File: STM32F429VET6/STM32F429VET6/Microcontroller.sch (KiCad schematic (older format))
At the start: 36 parts

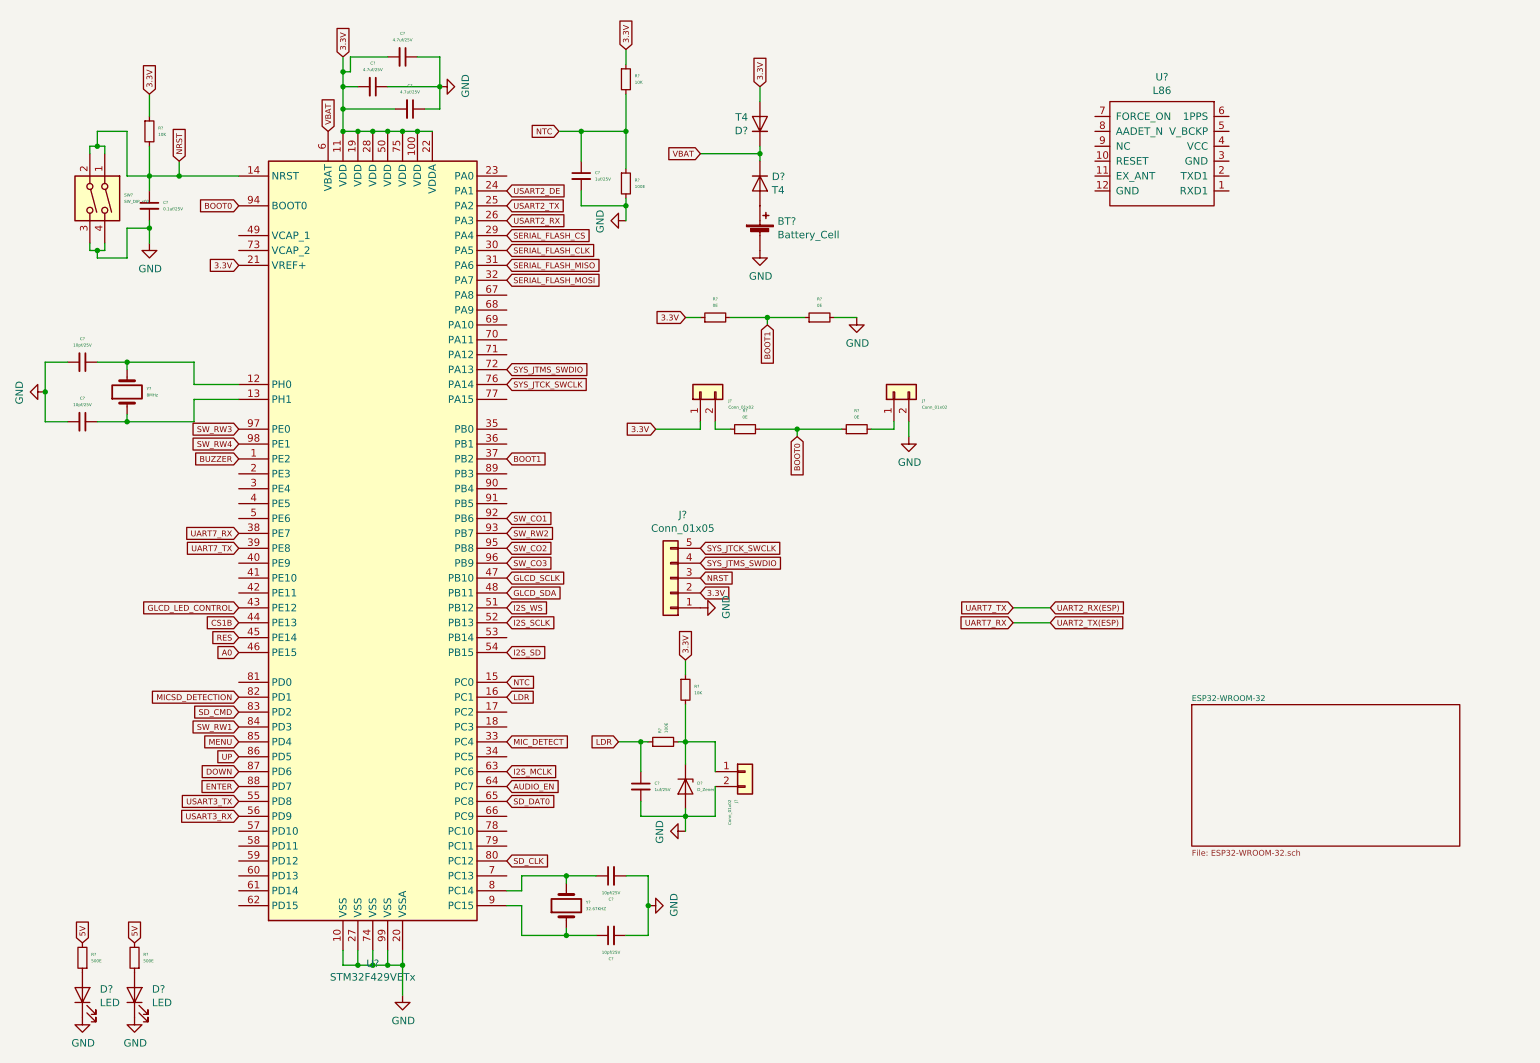
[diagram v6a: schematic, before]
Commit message: Completed GPS module connection
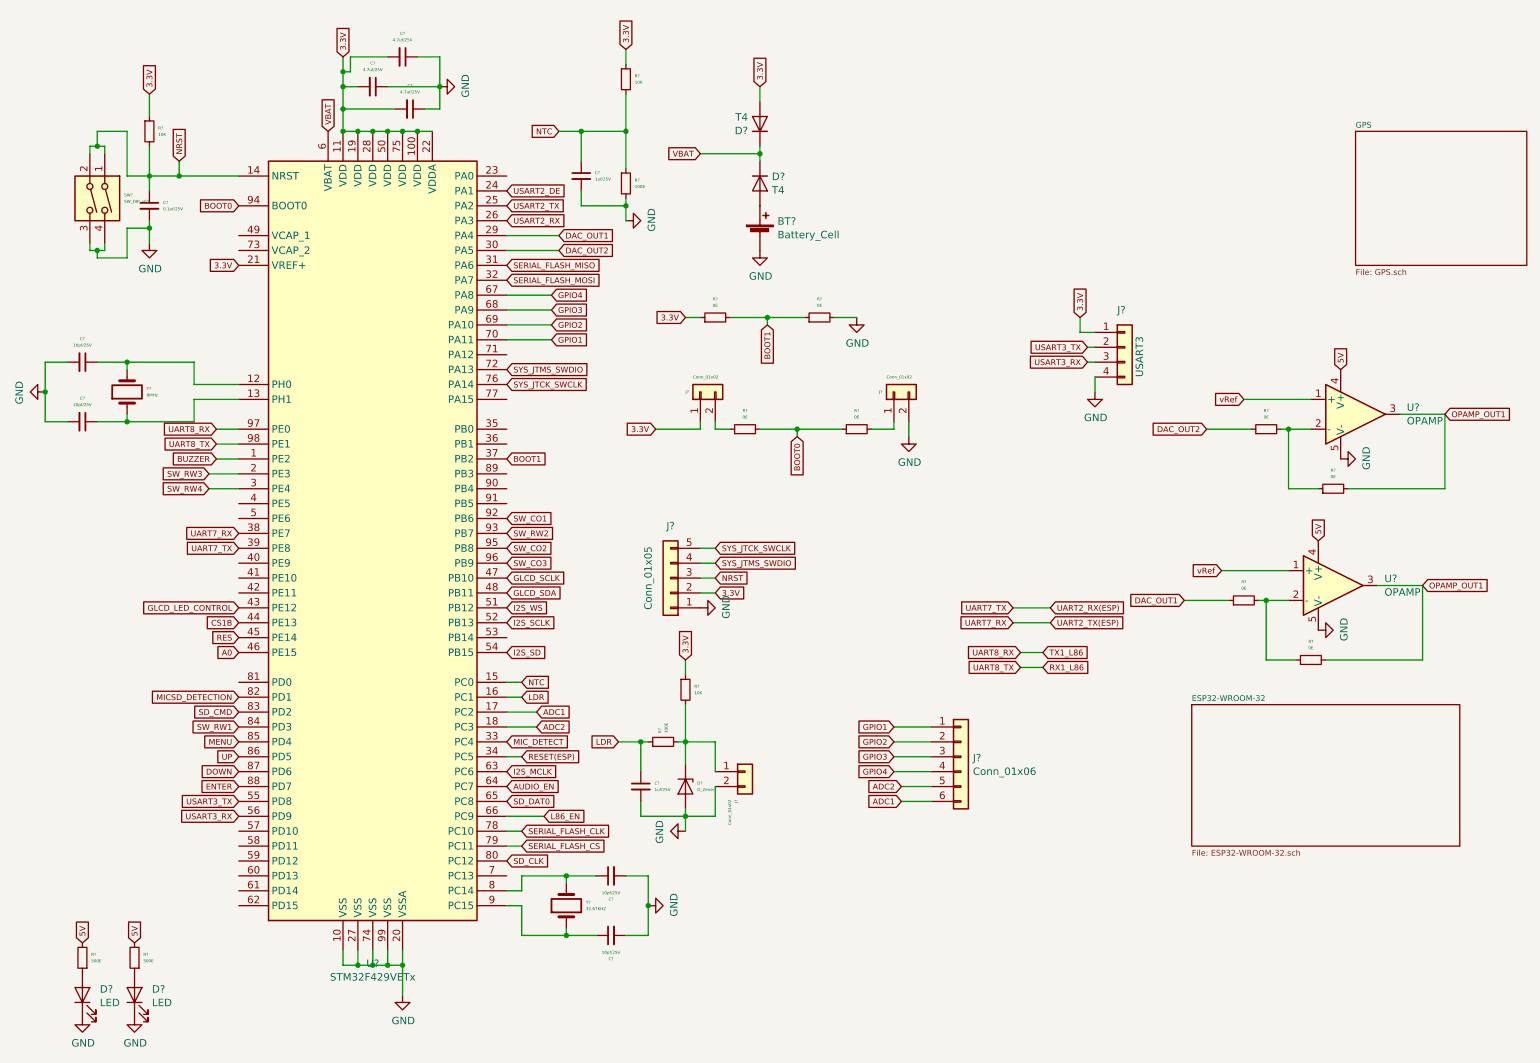
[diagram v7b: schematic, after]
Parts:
- removed U?: L86, Quectel_L86:Quectel_L86, symbol Quectel_L86:L86
- added J?: Conn_01x06, symbol Connector_Generic:Conn_01x06
- added J?: USART3, symbol Connector_Generic:Conn_01x04
- added R? (x4): 0E, Resistor_SMD:R_0805_2012Metric_Pad1.15x1.40mm_HandSolder, symbol Device:R_Small
- added U? (x2): OPAMP, symbol pspice:OPAMP
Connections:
- net 3.3V: now also J?.1 (Pin_1)
- net 5V: now also U?.4 (V+), U?.4 (V+)
- net GND: now also J?.4 (Pin_4), U?.5 (V-), U?.5 (V-)
- net SERIAL_FLASH_CLK: now also U?.78 (PC10); no longer U?.30 (PA5)
- net SERIAL_FLASH_CS: now also U?.79 (PC11); no longer U?.29 (PA4)
- net SW_RW3: now also U?.2 (PE3); no longer U?.97 (PE0)
- net SW_RW4: now also U?.3 (PE4); no longer U?.98 (PE1)
- net USART3_RX: now also J?.3 (Pin_3)
- net USART3_TX: now also J?.2 (Pin_2)
- net ADC1: now reaches U?.17 (PC2)
- net ADC1: now also J?.6 (Pin_6)
- net ADC2: now reaches U?.18 (PC3)
- net ADC2: now also J?.5 (Pin_5)
- net RESET(ESP): now reaches U?.34 (PC5)
- net L86_EN: now reaches U?.66 (PC9)
- net GPIO4: now reaches U?.67 (PA8)
- net GPIO4: now also J?.4 (Pin_4)
- net GPIO3: now reaches U?.68 (PA9)
- net GPIO3: now also J?.3 (Pin_3)
- net GPIO2: now reaches U?.69 (PA10)
- net GPIO2: now also J?.2 (Pin_2)
- net GPIO1: now reaches U?.70 (PA11)
- net GPIO1: now also J?.1 (Pin_1)
- new net: R?.1, R?.2, U?.2 (-) (x2)
- new net DAC_OUT1: R?.1, U?.29 (PA4)
- new net DAC_OUT2: R?.1, U?.30 (PA5)
- new net OPAMP_OUT1: R?.2, R?.2, U?.3, U?.3
- new net RX1_L86: U?.98 (PE1)
- new net TX1_L86: U?.97 (PE0)
- new net vRef: U?.1 (+), U?.1 (+)
